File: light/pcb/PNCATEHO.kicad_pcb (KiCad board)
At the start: 2 copper layers, 85.6 x 54 mm, 51 parts, among them J1 USB_C_Receptacle_USB2.0, SW11 Boot, SW12 Boot, U1 RP2040, U2 RT9013-33GB, U3 W25Q32JVSSIQ, U4 USBLC6-2SC6, Y1 12MHz

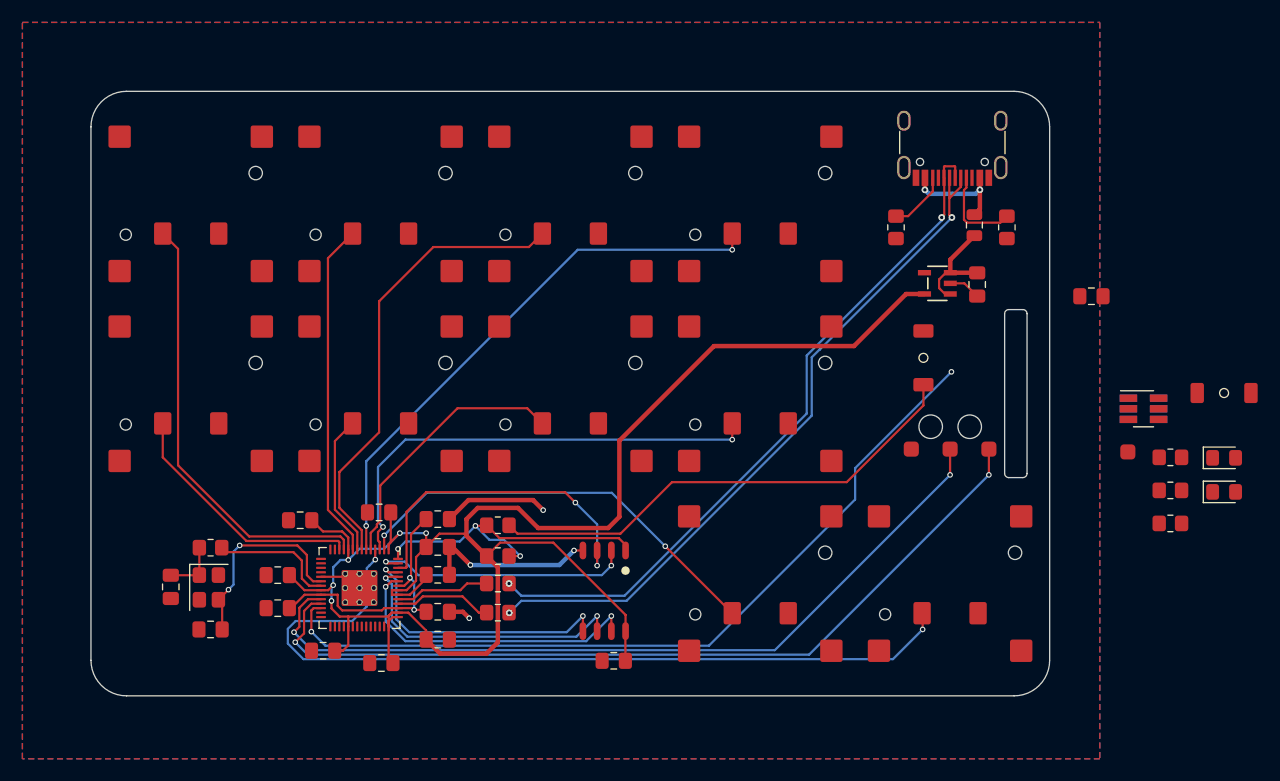
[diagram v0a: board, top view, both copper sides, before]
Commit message: * components moved closer to each other;  * rerouted with esd protection;  * fixed usb data differential pair length;  * changed design to be like a credit card;
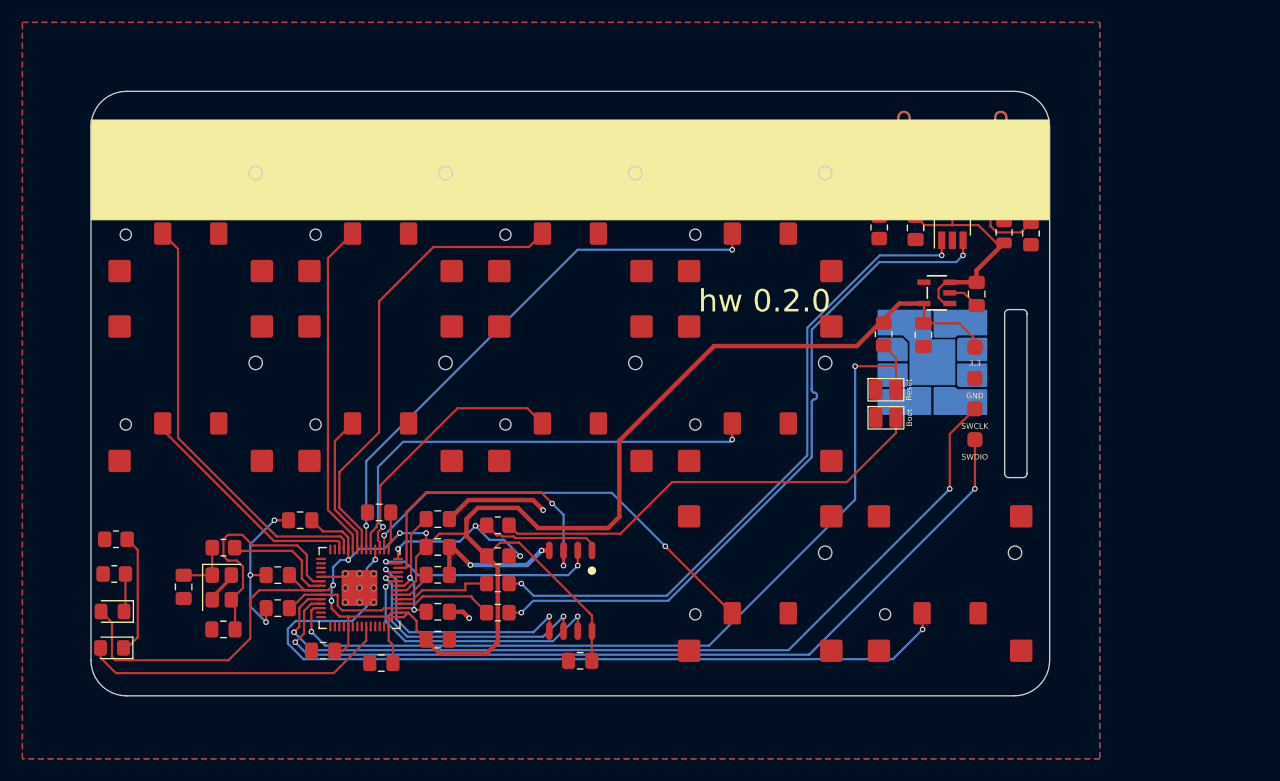
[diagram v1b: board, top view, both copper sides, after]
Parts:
- added C17: 100nF, PNCATEHO:C_0805_2012Metric_Pad1.18x1.45mm_HandSolder, F.Cu at (171.8, 88.4)
- added REF**: CreditCardPads, PNCATEHO:CreditCardPads, F.Cu at (173.3, 100.4)
- D1: value Red -> RED; footprint PNCATEHO:D_0805_2012Metric_Pad1.15x1.40mm_HandSolder -> PNCATEHO:LED_0805_2012Metric_Pad1.15x1.40mm_HandSolder
- D2: value Blue -> BLUE; footprint PNCATEHO:D_0805_2012Metric_Pad1.15x1.40mm_HandSolder -> PNCATEHO:LED_0805_2012Metric_Pad1.15x1.40mm_HandSolder
- SW12: value Boot -> Reset
- moved D2 100.3 mm to (100.0, 125.9), turned to 180 degrees
- moved D1 100.2 mm to (100.1, 122.7), turned to 180 degrees
- moved R9 94.6 mm to (100.2, 119.3)
- moved R10 94.2 mm to (100.4, 116.2)
- moved SW12 30.2 mm to (169.2, 102.8)
- moved R8 27.9 mm to (168.9, 97.9), turned to 90 degrees
- moved U4 23.7 mm to (175.1, 88.2), turned to 90 degrees
- moved TP4 16.5 mm to (177.1, 99.1)
- moved C2 15.4 mm to (172.5, 98.0), turned to -90 degrees
- moved TP1 8.50 mm to (177.1, 101.8)
- moved SW11 6.31 mm to (169.2, 105.3), turned to 0 degrees
- moved TP3 4.23 mm to (177.1, 104.5)
- moved C3 3.00 mm to (141.8, 127.0)
- moved U3 3.00 mm to (141.0, 120.8)
- moved F1 2.73 mm to (179.7, 88.8)
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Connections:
- net Net-(U1-USB_DM) renamed /RP2040_D-
- net Net-(U1-USB_DP) renamed /RP2040_D+
- net USB_D+ renamed USB_PROTECTED_D+
- net USB_D- renamed USB_PROTECTED_D-
- J1 pad A6: USBBP -> USBD+
- J1 pad A7: USBBN -> USBD-
- J1 pad B6: USBBP -> USBD+
- J1 pad B7: USBBN -> USBD-
- R8 pad 1: +3V3 -> ~{RESET}
- R8 pad 2: Net-(R8-Pad2) -> +3V3
- SW12 pad 2: Net-(R8-Pad2) -> ~{RESET}
- U4 pad 4: USBBP -> USBD-
- U4 pad 6: USBBN -> USBD+
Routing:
- net +3V3: track 162.1 -> 196.1 mm
- net STATE_LED: track 0.00 -> 27.6 mm
- net GND: track 32.4 -> 46.7 mm, vias 4 -> 7
- net Net-(D2-K): track 0.00 -> 10.8 mm
- net +5V: track 9.85 -> 20.4 mm
- net USBD-: track 0.00 -> 6.01 mm
- net USBD+: track 0.00 -> 5.99 mm
- net SWCLK: track 72.7 -> 77.9 mm
- net ~{RESET}: track 72.3 -> 77.2 mm
- net BOOT: track 43.9 -> 39.9 mm
- net Net-(D1-K): track 0.00 -> 3.40 mm
- net XIN: track 18.2 -> 21.5 mm, vias 2 -> 0
- net USB_PROTECTED_D+: track 62.9 -> 59.7 mm
- net QSPI_D0: track 25.5 -> 22.3 mm
- net QSPI_D3: track 27.5 -> 24.5 mm
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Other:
- outline, holes or cut-outs redrawn
- board text added: "08/25"
- board text added: "2025 0800 3333 0020"
- board text added: "PNCATEHO Welcome"
- board text added: "RPi"
- board text added: "VALID FROM"
- board text added: "hw 0.2.0"
- board text added: "inspired by aroum's original design"
- board text added: "pcb: turtle & inpdiy"
- board text removed: "ORIGINAL DESIGNER: AROUM'S"
- board text removed: "PCB DESIGN BY: TURTLE INPUDIY"
- board text removed: "VER: 020"
- board text removed: "Valid: 08.25"
- board text removed: "pcb by: turtle & inpdiy"

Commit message: update design
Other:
- board text added: "PNCATEHO"
- board text added: "PWV: 020"
- board text added: "VALID THRU"
- board text added: "Welcome"
- board text removed: "PNCATEHO Welcome"
- board text removed: "VALID FROM"
- board text removed: "hw 0.2.0"
